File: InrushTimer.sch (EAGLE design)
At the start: 71 parts, among them IC1 TLC272D, IC2 555, IC3 4076N, Q1 TIP41C, Q2 TRANSISTOR-FET_2N7002, Q3 TRANSISTOR-FET_2N7002, Q4 TRANSISTOR-FET_2N7002, Q5 TRANSISTOR-FET_2N7002, U1 ROHM_BY_ELEMENT14_BATCH_1_BU4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

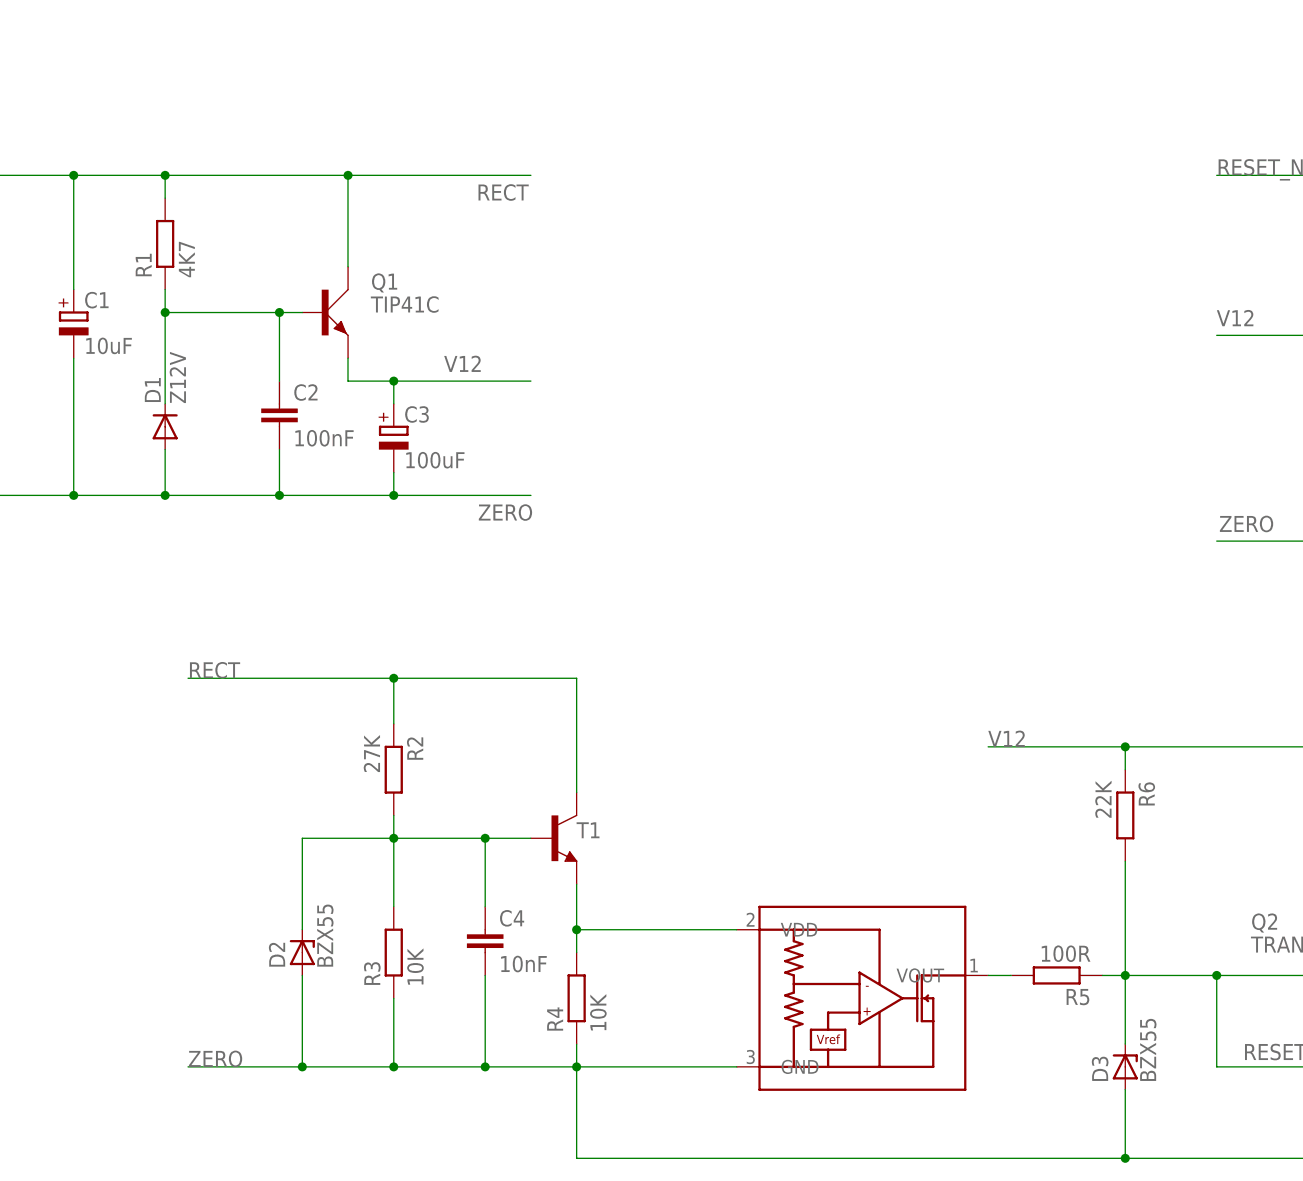
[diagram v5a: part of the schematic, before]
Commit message: Updated zener model and added annotation on schematic.
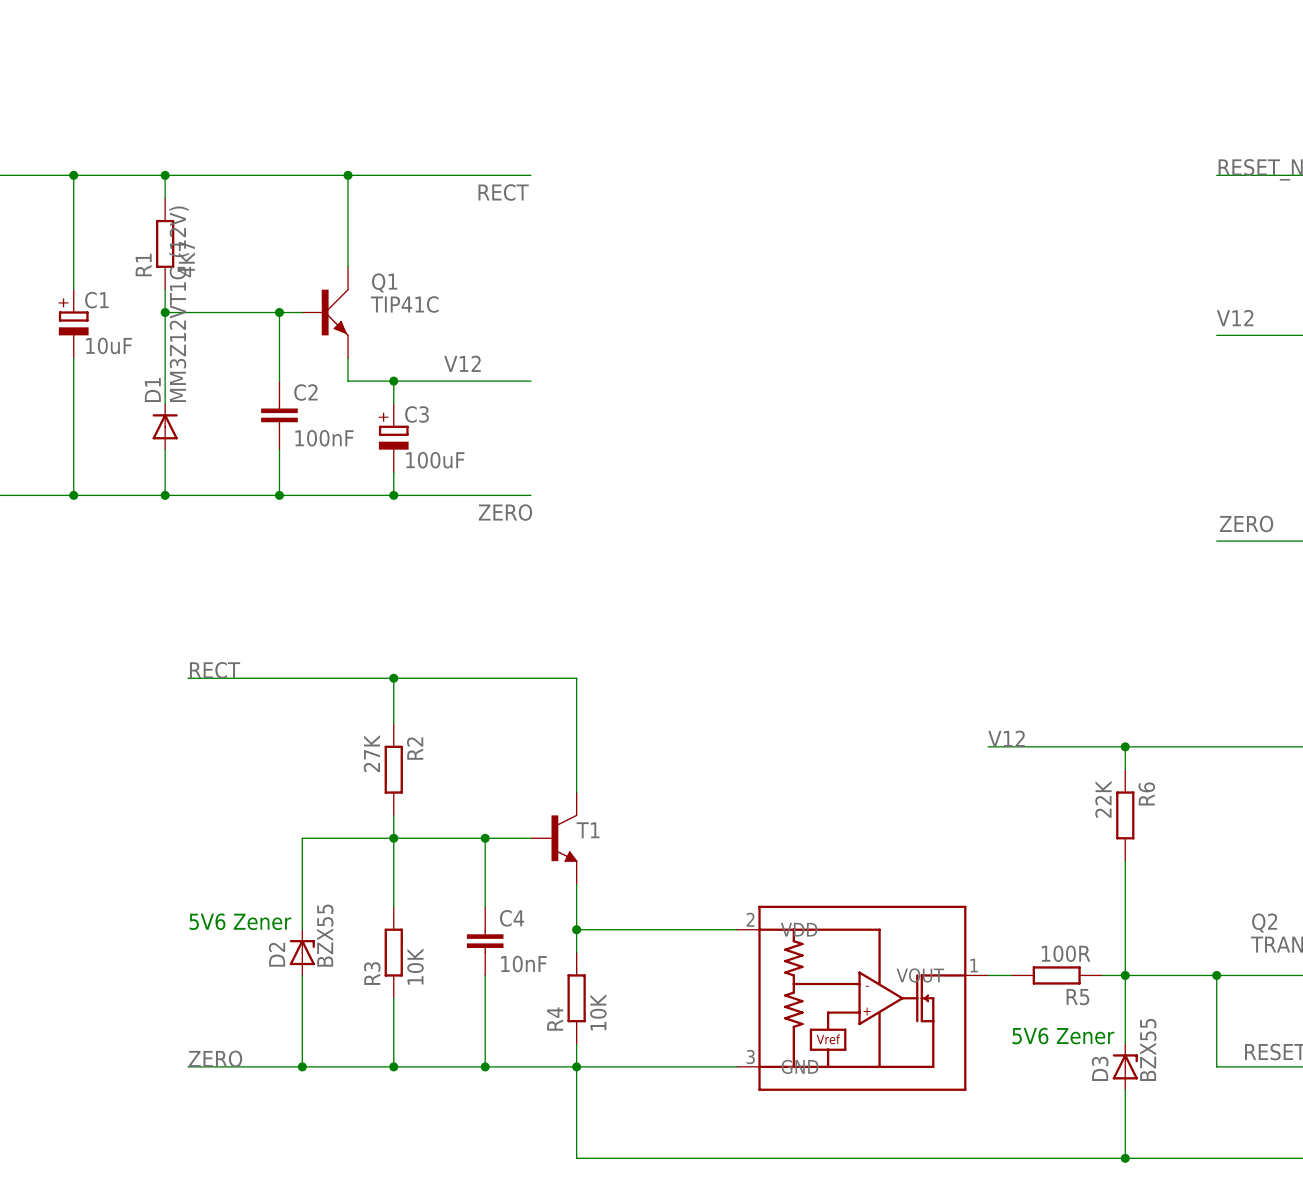
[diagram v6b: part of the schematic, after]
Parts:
- D1: value Z12V -> MM3Z12VT1G (12V)
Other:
- note added: "5V6 Zener"
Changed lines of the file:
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@@
 <grid distance="0.1" unitdist="inch" unit="inch" style="lines" multiple="1" display="no" altdistance="0.01" altunitdist="inch" altunit="inch"/>
 <layers>
-<layer number="1" name="Top" color="4" fill="1" visible="yes" active="no"/>
-<layer number="2" name="Route2" color="1" fill="3" visible="yes" active="no"/>
-<layer number="3" name="Route3" color="4" fill="3" visible="yes" active="no"/>
-<layer number="14" name="Route14" color="1" fill="6" visible="yes" active="no"/>
-<layer number="15" name="Route15" color="4" fill="6" visible="yes" active="no"/>
-<layer number="16" name="Bottom" color="1" fill="1" visible="yes" active="no"/>
-<layer number="17" name="Pads" color="2" fill="1" visible="yes" active="no"/>
-<layer number="18" name="Vias" color="2" fill="1" visible="yes" active="no"/>
-<layer number="19" name="Unrouted" color="6" fill="1" visible="yes" active="no"/>
-<layer number="20" name="Dimension" color="24" fill="1" visible="yes" active="no"/>
-<layer number="21" name="tPlace" color="15" fill="1" visible="yes" active="no"/>
-<layer number="22" name="bPlace" color="14" fill="1" visible="yes" active="no"/>
-<layer number="23" name="tOrigins" color="15" fill="1" visible="yes" active="no"/>
-<layer number="24" name="bOrigins" color="15" fill="1" visible="yes" active="no"/>
-<layer number="25" name="tNames" color="7" fill="1" visible="yes" active="no"/>
-<layer number="26" name="bNames" color="7" fill="1" visible="yes" active="no"/>
-<layer number="27" name="tValues" color="7" fill="1" visible="yes" active="no"/>
-<layer number="28" name="bValues" color="7" fill="1" visible="yes" active="no"/>
+<layer number="1" name="Top" color="4" fill="1" visible="no" active="no"/>
+<layer number="2" name="Route2" color="1" fill="3" visible="no" active="no"/>
+<layer number="3" name="Route3" color="4" fill="3" visible="no" active="no"/>
+<layer number="14" name="Route14" color="1" fill="6" visible="no" active="no"/>
+<layer number="15" name="Route15" color="4" fill="6" visible="no" active="no"/>
+<layer number="16" name="Bottom" color="1" fill="1" visible="no" active="no"/>
+<layer number="17" name="Pads" color="2" fill="1" visible="no" active="no"/>
+<layer number="18" name="Vias" color="2" fill="1" visible="no" active="no"/>
+<layer number="19" name="Unrouted" color="6" fill="1" visible="no" active="no"/>
+<layer number="20" name="Dimension" color="24" fill="1" visible="no" active="no"/>
+<layer number="21" name="tPlace" color="15" fill="1" visible="no" active="no"/>
+<layer number="22" name="bPlace" color="14" fill="1" visible="no" active="no"/>
+<layer number="23" name="tOrigins" color="15" fill="1" visible="no" active="no"/>
+<layer number="24" name="bOrigins" color="15" fill="1" visible="no" active="no"/>
+<layer number="25" name="tNames" color="7" fill="1" visible="no" active="no"/>
+<layer number="26" name="bNames" color="7" fill="1" visible="no" active="no"/>
+<layer number="27" name="tValues" color="7" fill="1" visible="no" active="no"/>
+<layer number="28" name="bValues" color="7" fill="1" visible="no" active="no"/>
 <layer number="29" name="tStop" color="7" fill="3" visible="no" active="no"/>
 <layer number="30" name="bStop" color="7" fill="6" visible="no" active="no"/>
@@
 <layer number="35" name="tGlue" color="7" fill="4" visible="no" active="no"/>
 <layer number="36" name="bGlue" color="7" fill="5" visible="no" active="no"/>
-<layer number="37" name="tTest" color="7" fill="1" visible="yes" active="no"/>
-<layer number="38" name="bTest" color="7" fill="1" visible="yes" active="no"/>
+<layer number="37" name="tTest" color="7" fill="1" visible="no" active="no"/>
+<layer number="38" name="bTest" color="7" fill="1" visible="no" active="no"/>
 <layer number="39" name="tKeepout" color="4" fill="11" visible="no" active="no"/>
 <layer number="40" name="bKeepout" color="1" fill="11" visible="no" active="no"/>
@@
 <layer number="44" name="Drills" color="7" fill="1" visible="no" active="no"/>
 <layer number="45" name="Holes" color="7" fill="1" visible="no" active="no"/>
-<layer number="46" name="Milling" color="3" fill="1" visible="yes" active="no"/>
-<layer number="47" name="Measures" color="7" fill="1" visible="yes" active="no"/>
-<layer number="48" name="Document" color="7" fill="1" visible="yes" active="no"/>
-<layer number="49" name="Reference" color="7" fill="1" visible="yes" active="no"/>
-<layer number="50" name="dxf" color="7" fill="1" visible="yes" active="no"/>
-<layer number="51" name="tDocu" color="6" fill="1" visible="yes" active="no"/>
-<layer number="52" name="bDocu" color="7" fill="1" visible="yes" active="no"/>
-<layer number="53" name="tGND_GNDA" color="7" fill="9" visible="yes" active="no"/>
-<layer number="54" name="bGND_GNDA" color="1" fill="9" visible="yes" active="no"/>
-<layer number="56" name="wert" color="7" fill="1" visible="yes" active="no"/>
+<layer number="46" name="Milling" color="3" fill="1" visible="no" active="no"/>
+<layer number="47" name="Measures" color="7" fill="1" visible="no" active="no"/>
+<layer number="48" name="Document" color="7" fill="1" visible="no" active="no"/>
+<layer number="49" name="Reference" color="7" fill="1" visible="no" active="no"/>
+<layer number="50" name="dxf" color="7" fill="1" visible="no" active="no"/>
+<layer number="51" name="tDocu" color="6" fill="1" visible="no" active="no"/>
+<layer number="52" name="bDocu" color="7" fill="1" visible="no" active="no"/>
+<layer number="53" name="tGND_GNDA" color="7" fill="9" visible="no" active="no"/>
+<layer number="54" name="bGND_GNDA" color="1" fill="9" visible="no" active="no"/>
+<layer number="56" name="wert" color="7" fill="1" visible="no" active="no"/>
 <layer number="90" name="Modules" color="5" fill="1" visible="yes" active="yes"/>
 <layer number="91" name="Nets" color="2" fill="1" visible="yes" active="yes"/>
@@
 </classes>
 <parts>
-<part name="D1" library="diode" deviceset="DIODE-" device="SOD323-R" value="Z12V"/>
+<part name="D1" library="diode" deviceset="DIODE-" device="SOD323-R" value="MM3Z12VT1G (12V)"/>
 <part name="C1" library="rcl" deviceset="CPOL-EU" device="E2-5" value="10uF"/>
 <part name="C3" library="rcl" deviceset="CPOL-EU" device="E2.5-7" value="100uF"/>
@@
 <sheet>
 <plain>
+<text x="-96.52" y="-73.66" size="1.778" layer="91">5V6 Zener</text>
+<text x="-5.08" y="-86.36" size="1.778" layer="91">5V6 Zener</text>
 </plain>
 <instances>

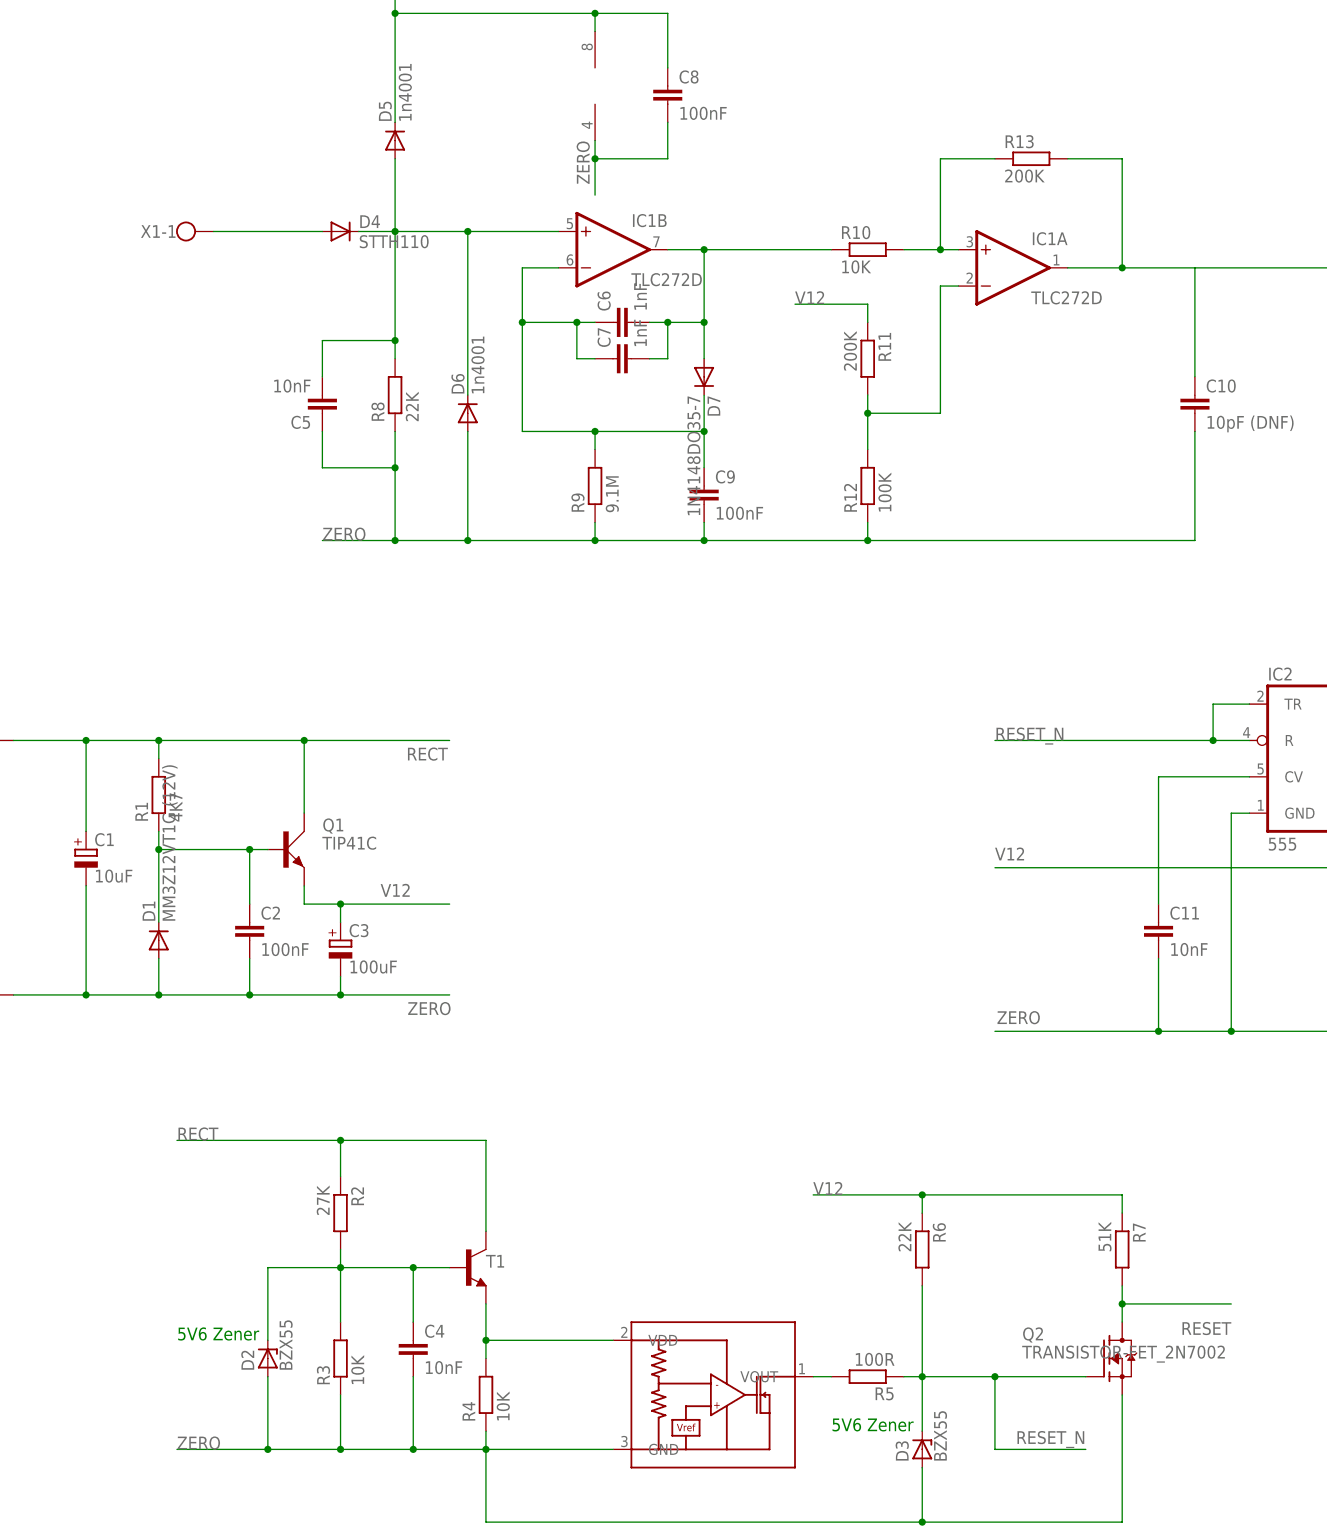
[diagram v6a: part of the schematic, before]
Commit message: Re-layed out peak detector, supply and reset generator.
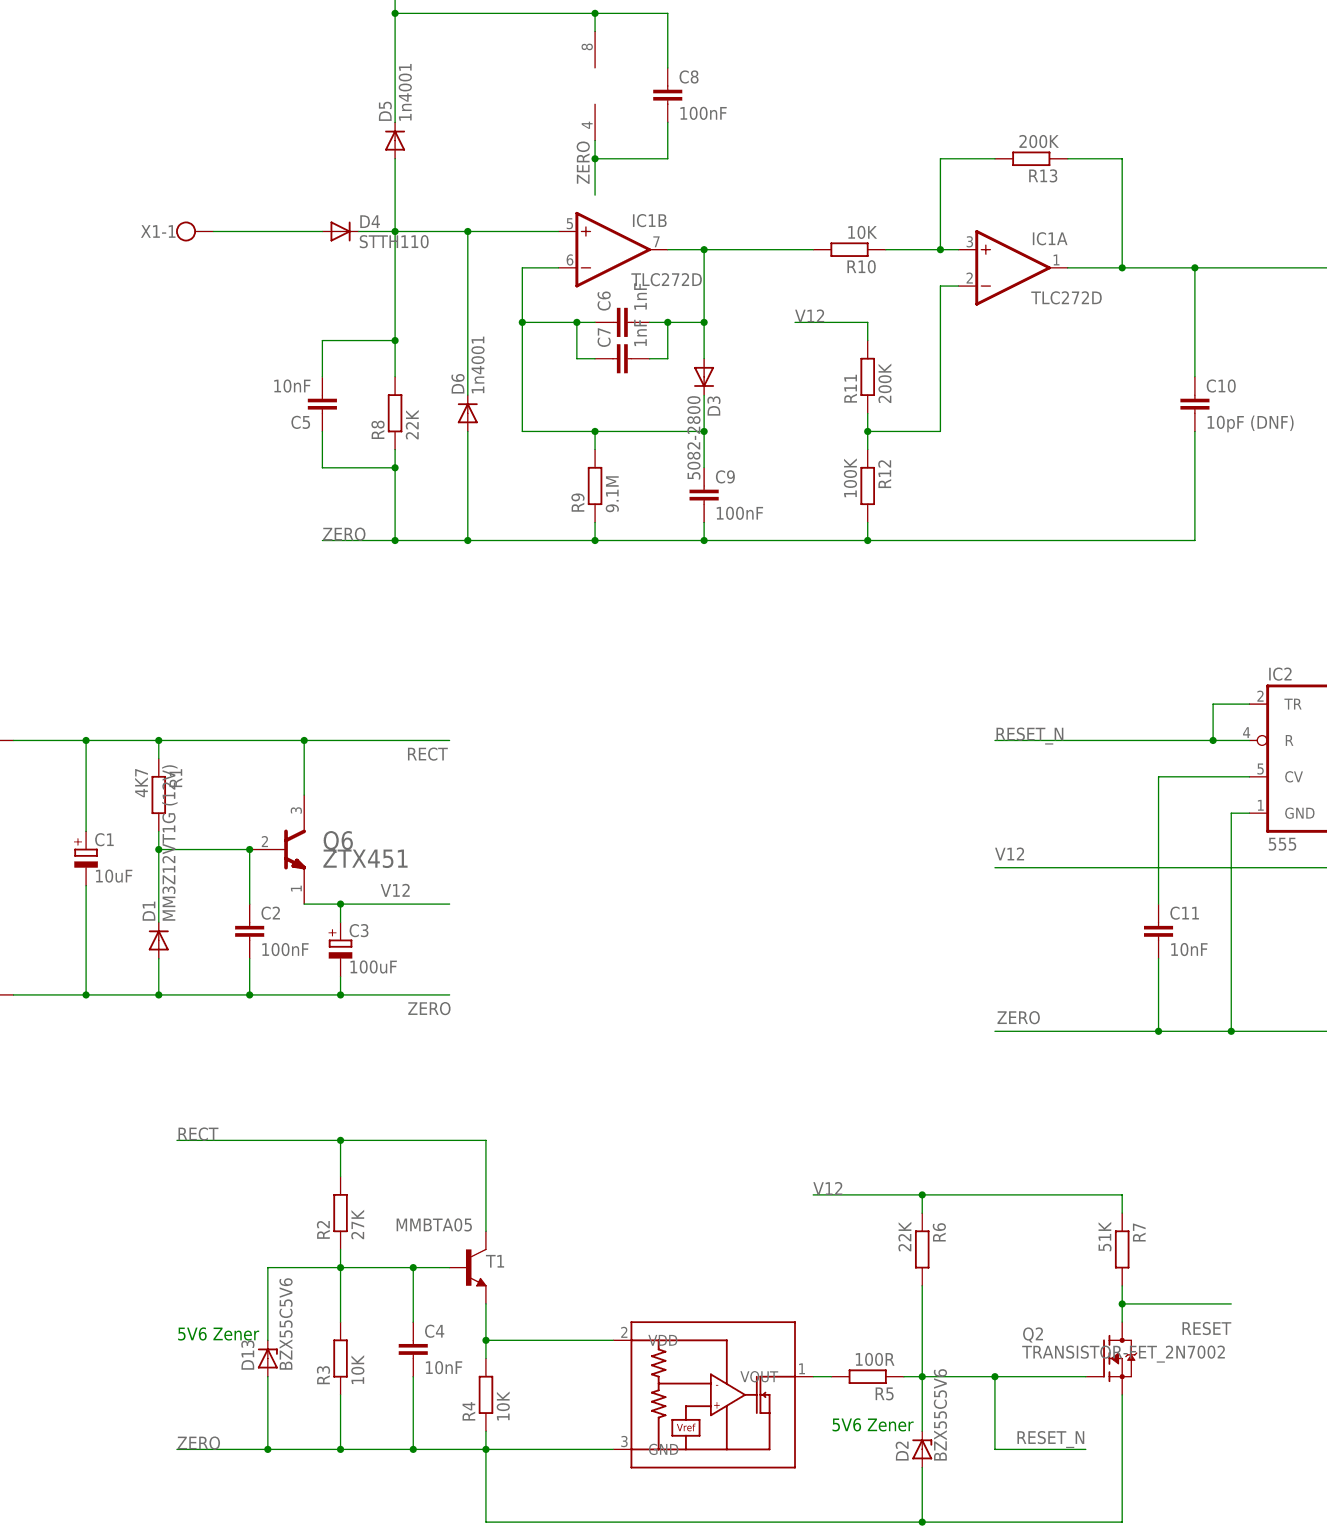
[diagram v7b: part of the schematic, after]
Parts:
- removed D7: 1N4148DO35-7, diode:1N4148DO35-7
- removed Q1: TIP41C, transistor-power:TIP41C
- added D13: BZX55C5V6, diode:ZENER-DIODEDO34-7
- added Q6: DIODES_ZTX451DIODES_ZTX451_0_0, Diodes - ZTX451:DIODES_ZTX451DIODES_ZTX451_0_0
- C8: device rcl:C-EUC1206K -> rcl:C-EUC0805
- D2: value BZX55 -> BZX55C5V6; device diode:BZX55 -> diode:ZENER-DIODEDO34-7
- D3: value BZX55 -> 5082-2800; device diode:BZX55 -> diode:DIODE-DO34-7
- D4: device diode:DIODE-DO41-10 -> diode:DIODE-DO41-7.6
- D5, D6: device diode:DIODE-DO41-10 -> diode:DIODE-DP41-10V
- R10: device rcl:R-EU_R0805 -> rcl:R-EU_0207/10
- R2, R5, R7: device rcl:R-EU_0207/2V -> rcl:R-EU_0207/7
- R9: device rcl:R-EU_0207/10 -> rcl:R-EU_0204/7
- T1: value (none) -> MMBTA05
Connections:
- removed net HYST: IC1A.-IN, R11.2, R12.2
- new net THRESH: IC1A.-IN, R11.1, R12.1
- net N$14: now also D13.C, R2.1; no longer D2.C, R2.2
- net N$26: now also R10.1, R13.2; no longer R10.2, R13.1
- net N$7: now also D3.A, R10.2; no longer D7.A, R10.1
- net N$8: now also Q6.B, R1.2; no longer Q1.B, R1.1
- net N$9: now also D3.C; no longer D7.C
- net PEAK: now also R13.1; no longer R13.2
- net RECT: now also Q6.C, R1.1, R2.2; no longer Q1.C, R1.2, R2.1
- net RESET_N: now also D2.C; no longer D3.C
- net V12: now also Q6.E, R11.2; no longer Q1.E, R11.1
- net ZERO: now also D13.A, R12.2; no longer D3.A, R12.1
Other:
- moved on the sheet: R1, R10, R11, R12, R13, R2, R8
